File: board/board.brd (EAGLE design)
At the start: 94 x 44.5 mm, 64 parts, among them Q2 ULN2003AD

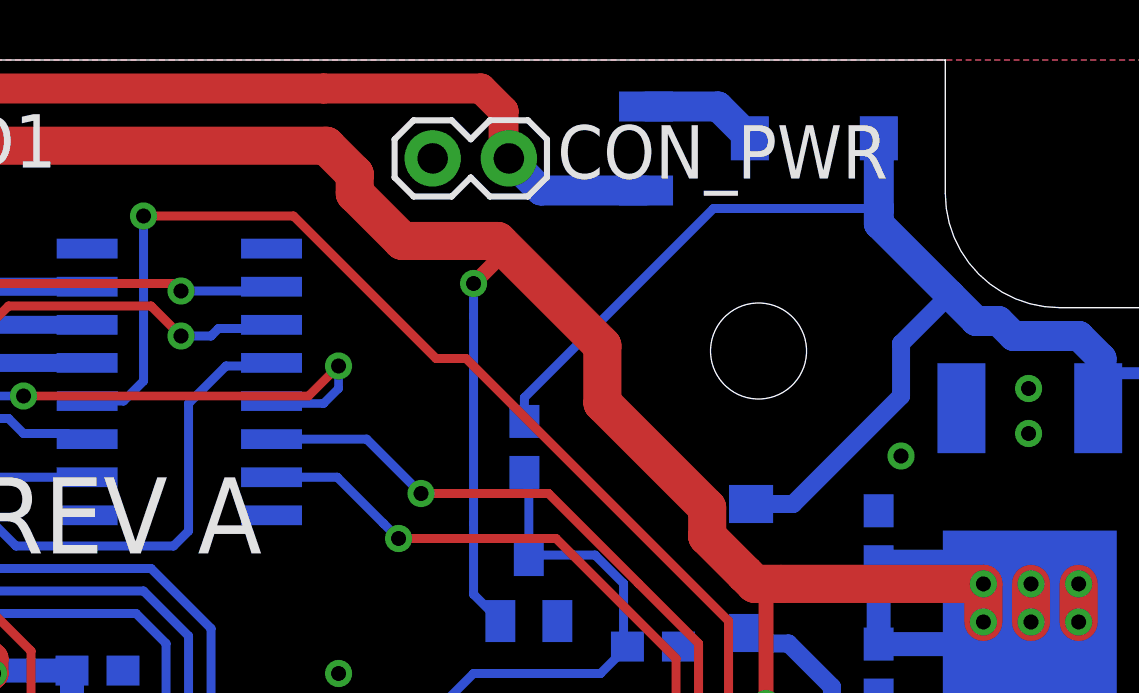
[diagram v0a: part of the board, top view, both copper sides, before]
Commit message: Adding TVS Diode
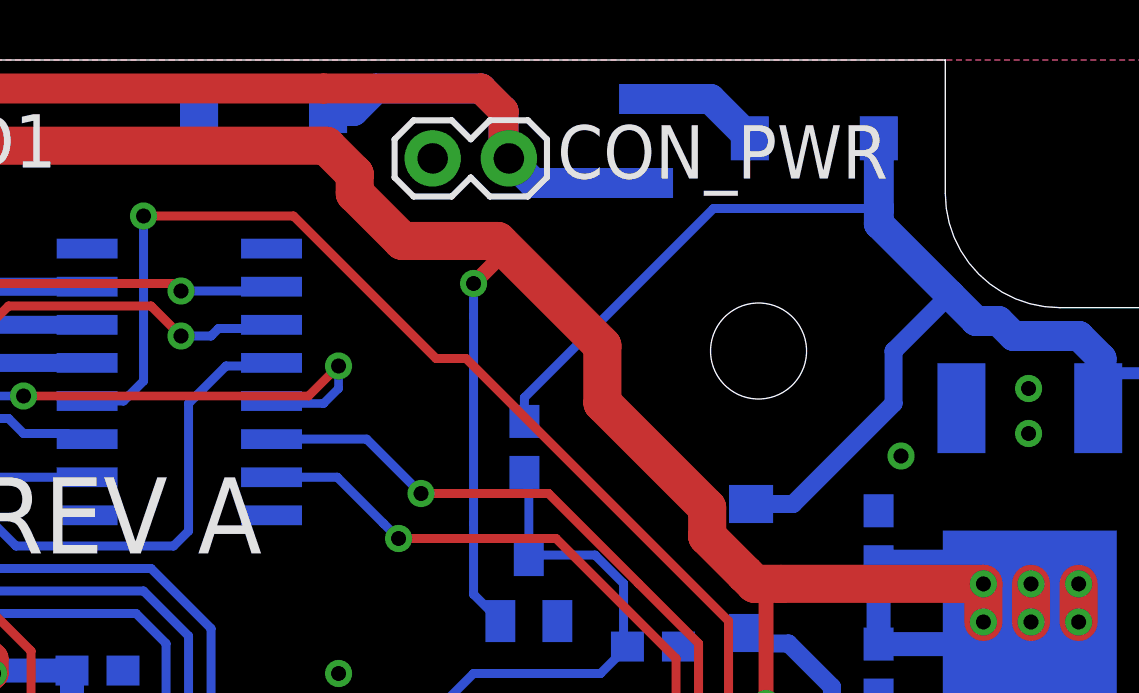
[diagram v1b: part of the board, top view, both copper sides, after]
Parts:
- added TVS1: SMAJ15CA, SparkFun-DiscreteSemi:SMA-DIODE
- moved F1 0.25 mm to (75.8, 41.8)
- renumbered MCU to STM32
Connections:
- net +12V: now also TVS1.C
- net GND: now also TVS1.A
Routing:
- net +12V: track 95.1 -> 103.1 mm

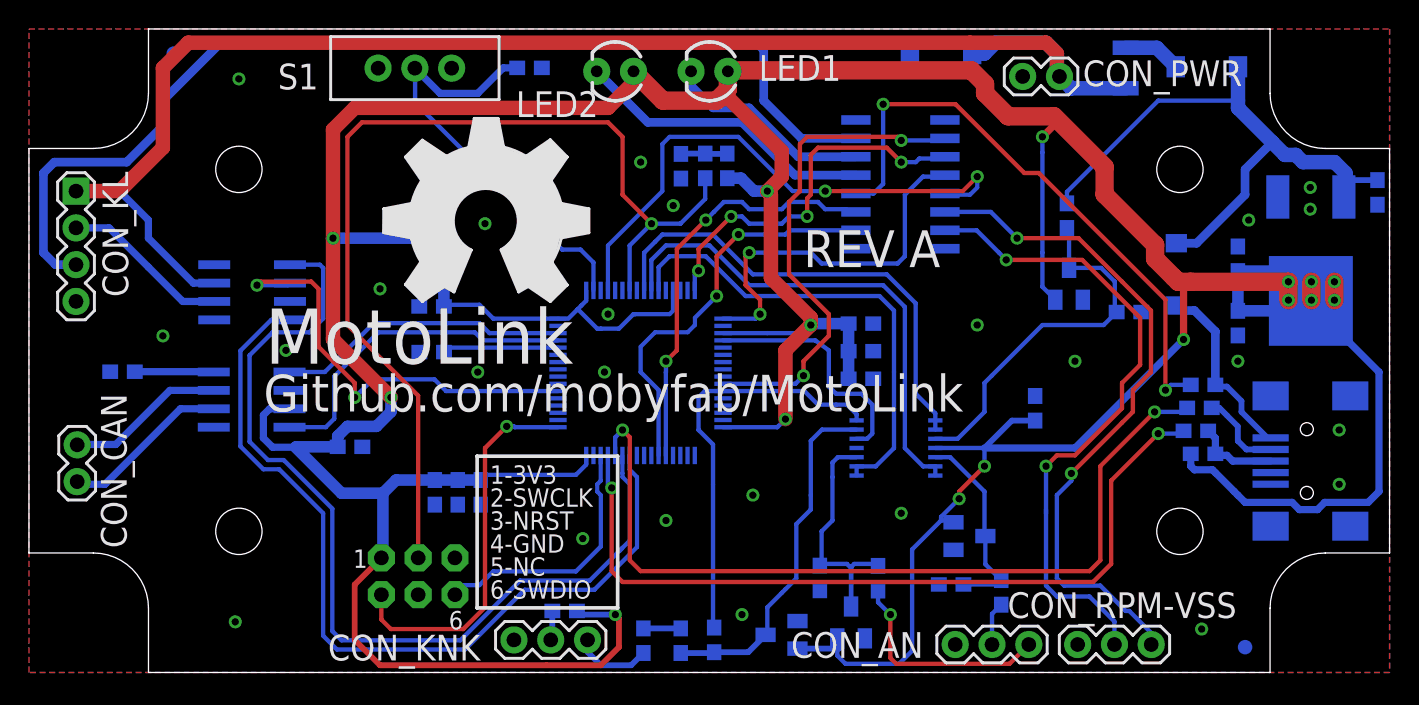
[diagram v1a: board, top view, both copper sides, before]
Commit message: TVS Diode changes, Adding pull-ups to K-line, updated K-line IC
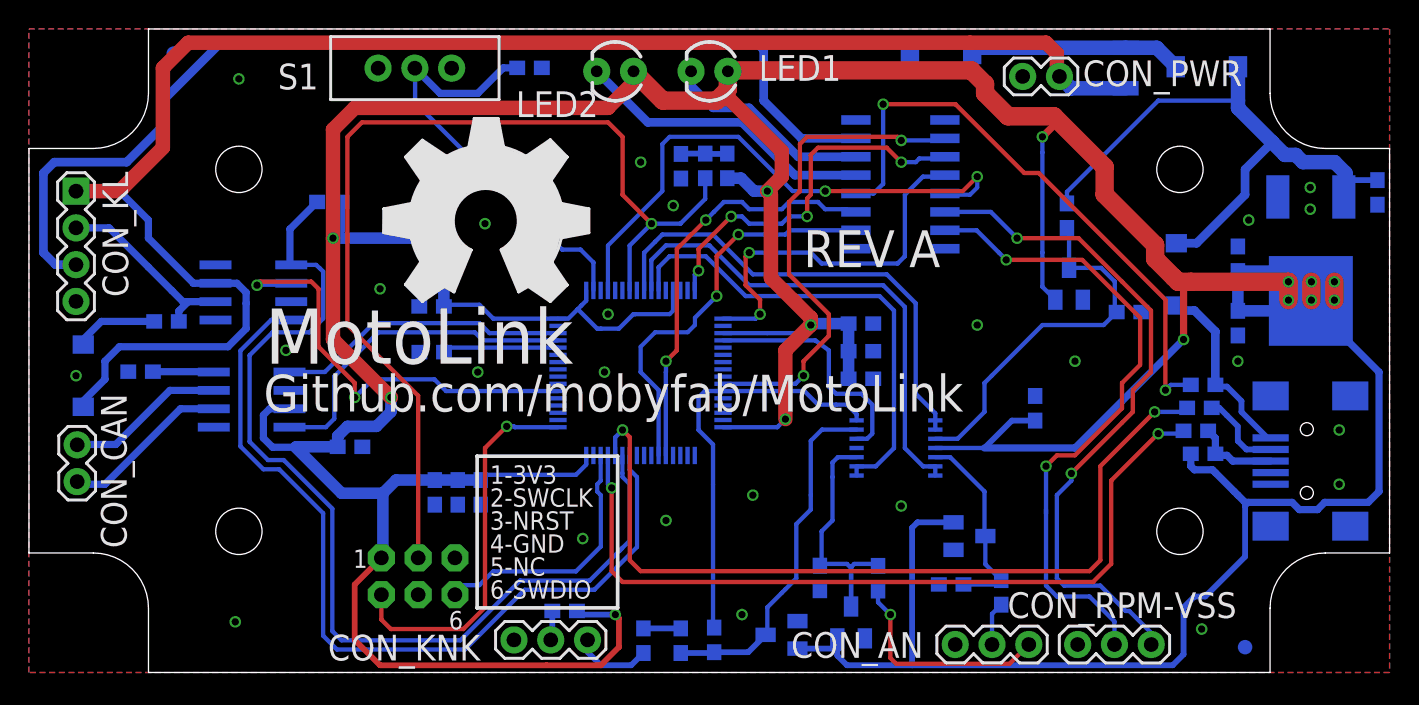
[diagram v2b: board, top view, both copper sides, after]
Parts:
- removed IC_KL: MCP2004, misc:SO08
- added D6: (no value), SparkFun-DiscreteSemi:SMA-DIODE
- added IC_KLINE: MCP2004, misc:SO08
- added R13: 1K, SparkFun-Resistors:0603-RES
- added R2: 4.7K, SparkFun-Resistors:0603-RES
- moved R3 1.25 mm to (7.71, 20.8)
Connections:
- new net N$13: D6.C, R13.2
- net +12V: now also D6.A, IC_KLINE.7; no longer IC_KL.7, TVS1.C
- net +3V3: now also R2.2
- net GND: now also IC_KLINE.5; no longer IC_KL.5
- net K-LINE: now also IC_KLINE.6, R13.1; no longer IC_KL.6
- net KL-CS: now also IC_KLINE.2; no longer IC_KL.2
- net N$9: now also TVS1.C
- net UART_RXD: now also IC_KLINE.1, R2.1; no longer IC_KL.1
- net UART_TXD: now also IC_KLINE.4; no longer IC_KL.4
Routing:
- net +3V3: track 371.7 -> 401.3 mm, vias 16 -> 14
- net +12V: track 103.1 -> 114.7 mm
- net N$9: track 4.00 -> 14.8 mm
- net N$13: track 0.00 -> 6.26 mm
- net UART_RXD: track 64.0 -> 68.9 mm
- net K-LINE: track 11.7 -> 13.4 mm
- net N$8: track 5.47 -> 4.22 mm

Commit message: Minor fixes
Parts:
- moved D6 1.50 mm to (2.25, 20.5)
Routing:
- net +12V: track 114.7 -> 116.2 mm
- net N$13: track 6.26 -> 7.06 mm
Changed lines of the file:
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@@
 </class>
 </classes>
-<designrules name="SeeedStudio_2layer_DRU_no_angle_20140221">
+<designrules name="SeeedStudio_2layer_DRU_no_angle_20140221 *">
 <description language="de">&lt;b&gt;EAGLE Design Rules&lt;/b&gt;
 &lt;p&gt;
@@
 <param name="mdDrill" value="10mil"/>
 <param name="mdSmdStop" value="0mil"/>
-<param name="msWidth" value="6mil"/>
+<param name="msWidth" value="8mil"/>
 <param name="msDrill" value="12mil"/>
 <param name="msMicroVia" value="12mil"/>
@@
 </element>
 <element name="R15" library="SparkFun-Resistors" package="0603-RES" value="33R" x="80.5975" y="16.6925" smashed="yes" rot="MR0">
-<attribute name="NAME" x="75.9865" y="15.9545" size="1.778" layer="26" font="vector" ratio="16" rot="MR0"/>
+<attribute name="NAME" x="77.7365" y="15.9545" size="1.778" layer="26" font="vector" ratio="16" rot="MR0"/>
 <attribute name="VALUE" x="81.6135" y="15.5495" size="0.4064" layer="28" font="vector" rot="MR0"/>
 </element>
 <element name="R16" library="SparkFun-Resistors" package="0603-RES" value="33R" x="80.8475" y="18.28" smashed="yes" rot="MR0">
-<attribute name="NAME" x="76.2365" y="18.042" size="1.778" layer="26" font="vector" ratio="16" rot="MR0"/>
+<attribute name="NAME" x="78.2365" y="18.042" size="1.778" layer="26" font="vector" ratio="16" rot="MR0"/>
 <attribute name="VALUE" x="81.8635" y="17.137" size="0.4064" layer="28" font="vector" rot="MR0"/>
 </element>
@@
 <attribute name="VALUE" x="10.516" y="23.107" size="0.4064" layer="28" font="vector" rot="MR0"/>
 </element>
-<element name="D6" library="SparkFun-DiscreteSemi" package="SMA-DIODE" value="" x="3.75" y="20.5" smashed="yes" rot="MR90">
-<attribute name="NAME" x="0.401" y="18.964" size="1.778" layer="26" font="vector" ratio="16" rot="MR90"/>
-<attribute name="VALUE" x="5.401" y="20.754" size="0.4064" layer="28" rot="MR90"/>
+<element name="D6" library="SparkFun-DiscreteSemi" package="SMA-DIODE" value="" x="2.25" y="20.5" smashed="yes" rot="MR90">
+<attribute name="NAME" x="3.901" y="18.964" size="1.778" layer="26" font="vector" ratio="16" rot="MR90"/>
+<attribute name="VALUE" x="3.901" y="20.754" size="0.4064" layer="28" rot="MR90"/>
 </element>
 </elements>
@@
 <via x="31.5" y="31" extent="1-16" drill="0.5"/>
 <via x="65.5" y="24" extent="1-16" drill="0.5"/>
-<via x="3.25" y="20.5" extent="1-16" drill="0.5"/>
+<via x="2.25" y="20.5" extent="1-16" drill="0.5"/>
 <via x="42.25" y="35.25" extent="1-16" drill="0.5"/>
 <contactref element="STM32" pad="12"/>
@@
 <wire x1="11.365" y1="26.885" x2="11.3525" y2="26.8975" width="0.5" layer="16"/>
 <contactref element="D6" pad="A"/>
-<wire x1="3.75" y1="18.35" x2="3.75" y2="18.75" width="0.5" layer="16"/>
-<wire x1="3.75" y1="18.75" x2="5.25" y2="20.25" width="0.5" layer="16"/>
-<wire x1="5.25" y1="20.25" x2="5.25" y2="21.5" width="0.5" layer="16"/>
-<wire x1="5.25" y1="21.5" x2="6.25" y2="22.5" width="0.5" layer="16"/>
-<wire x1="6.25" y1="22.5" x2="13.75" y2="22.5" width="0.5" layer="16"/>
+<wire x1="4.5" y1="19.5" x2="4.5" y2="21.25" width="0.5" layer="16"/>
+<wire x1="4.5" y1="21.25" x2="5.75" y2="22.5" width="0.5" layer="16"/>
+<wire x1="5.75" y1="22.5" x2="13.75" y2="22.5" width="0.5" layer="16"/>
 <wire x1="13.75" y1="22.5" x2="15" y2="23.75" width="0.5" layer="16"/>
 <wire x1="15" y1="23.75" x2="15" y2="25.5" width="0.5" layer="16"/>
@@
 <wire x1="14.365" y1="26.885" x2="15" y2="26.25" width="0.5" layer="16"/>
 <wire x1="15" y1="26.25" x2="15" y2="25.5" width="0.5" layer="16"/>
+<wire x1="2.25" y1="18.35" x2="3.35" y2="18.35" width="0.5" layer="16"/>
+<wire x1="3.35" y1="18.35" x2="4.5" y2="19.5" width="0.5" layer="16"/>
 </signal>
 <signal name="VCC">
@@
 <signal name="K-LINE">
 <contactref element="CON_KL" pad="2"/>
-<wire x1="3.25" y1="30.71" x2="5.54" y2="30.71" width="0.5" layer="16"/>
-<wire x1="5.54" y1="30.71" x2="8.25" y2="28" width="0.5" layer="16"/>
-<wire x1="10.6225" y1="25.6275" x2="9.875" y2="26.375" width="0.5" layer="16"/>
+<wire x1="3.25" y1="30.71" x2="5.29" y2="30.71" width="0.5" layer="16"/>
+<wire x1="5.29" y1="30.71" x2="8" y2="28" width="0.5" layer="16"/>
+<wire x1="10.3725" y1="25.6275" x2="9.625" y2="26.375" width="0.5" layer="16"/>
 <contactref element="IC_KLINE" pad="6"/>
-<wire x1="9.875" y1="26.375" x2="8.25" y2="28" width="0.5" layer="16"/>
-<wire x1="12.8838" y1="25.615" x2="11" y2="25.615" width="0.5" layer="16"/>
-<wire x1="11" y1="25.615" x2="10.635" y2="25.615" width="0.5" layer="16"/>
-<wire x1="10.635" y1="25.615" x2="10.6225" y2="25.6275" width="0.5" layer="16"/>
+<wire x1="9.625" y1="26.375" x2="8" y2="28" width="0.5" layer="16"/>
+<wire x1="12.8838" y1="25.615" x2="10.75" y2="25.615" width="0.5" layer="16"/>
+<wire x1="10.75" y1="25.615" x2="10.635" y2="25.615" width="0.5" layer="16"/>
+<wire x1="10.635" y1="25.615" x2="10.3725" y2="25.6275" width="0.5" layer="16"/>
 <contactref element="R13" pad="1"/>
-<wire x1="10.35" y1="24.25" x2="10.35" y2="24.965" width="0.5" layer="16"/>
-<wire x1="10.35" y1="24.965" x2="11" y2="25.615" width="0.5" layer="16"/>
+<wire x1="10.35" y1="24.25" x2="10.35" y2="25.215" width="0.5" layer="16"/>
+<wire x1="10.35" y1="25.215" x2="10.75" y2="25.615" width="0.5" layer="16"/>
 </signal>
 <signal name="KL-CS">
@@
 <wire x1="20" y1="22.5" x2="20" y2="26.5" width="0.3" layer="1"/>
 <wire x1="20" y1="26.5" x2="19.5" y2="27" width="0.3" layer="1"/>
-<wire x1="19.5" y1="27" x2="16" y2="27" width="0.3" layer="1"/>
-<wire x1="16" y1="27" x2="15.75" y2="26.75" width="0.3" layer="1"/>
-<via x="15.75" y="26.75" extent="1-16" drill="0.5"/>
+<wire x1="19.5" y1="27" x2="16.25" y2="27" width="0.3" layer="1"/>
+<wire x1="16.25" y1="27" x2="16" y2="27.25" width="0.3" layer="1"/>
+<via x="16" y="27.25" extent="1-16" drill="0.5"/>
 <contactref element="IC_KLINE" pad="2"/>
-<wire x1="18.1162" y1="26.885" x2="15.885" y2="26.885" width="0.5" layer="16"/>
-<wire x1="15.885" y1="26.885" x2="15.75" y2="26.75" width="0.5" layer="16"/>
+<wire x1="18.1162" y1="26.885" x2="16.385" y2="26.885" width="0.5" layer="16"/>
+<wire x1="16.385" y1="26.885" x2="16.365" y2="26.885" width="0.5" layer="16"/>
+<wire x1="16.365" y1="26.885" x2="16" y2="27.25" width="0.5" layer="16"/>
 </signal>
 <signal name="N$2">
@@
 <contactref element="R13" pad="2"/>
 <contactref element="D6" pad="C"/>
-<wire x1="3.75" y1="22.65" x2="3.4" y2="22.65" width="0.5" layer="16"/>
+<wire x1="2.25" y1="22.65" x2="3.4" y2="22.65" width="0.5" layer="16"/>
 <wire x1="3.4" y1="22.65" x2="5" y2="24.25" width="0.5" layer="16"/>
 <wire x1="5" y1="24.25" x2="8.65" y2="24.25" width="0.5" layer="16"/>
